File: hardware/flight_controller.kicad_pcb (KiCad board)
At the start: 6 copper layers, 50 x 50 mm, 81 parts, among them IC2 STM32F722RET6, IC3 W25Q128JVSIQ, J1 Conn_01x03, J2 Conn_01x08, J3 Conn_01x04, J4 Conn_01x04, J5 Conn_01x04, J6 USB4105-GF-A-060, Q1 TPRT9013-33GB, SW2 SW_SPST, U1 BMP581, U2 MP9943GQ-Z, U3 USBLC6-2P6, U4 MP9943GQ-Z, Y2 X322525MOB4SI

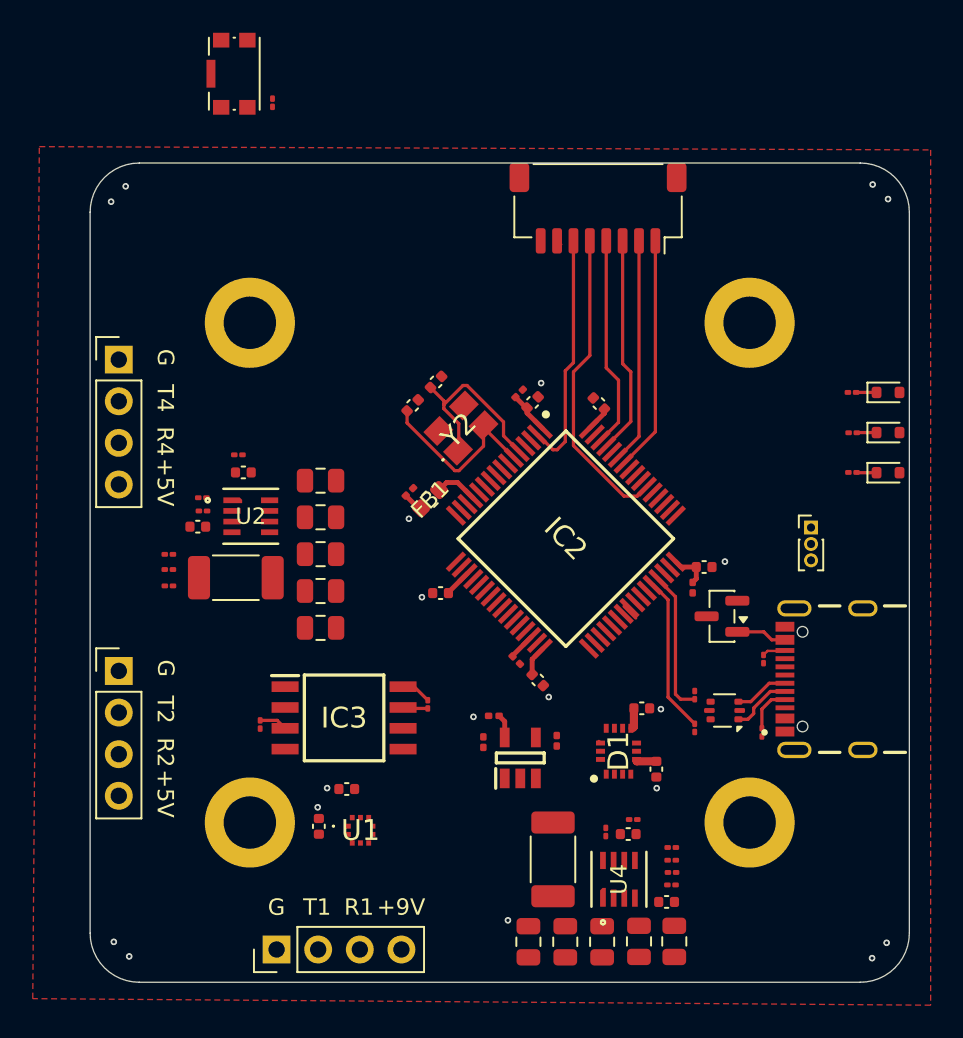
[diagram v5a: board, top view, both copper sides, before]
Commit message: redefined signal layout
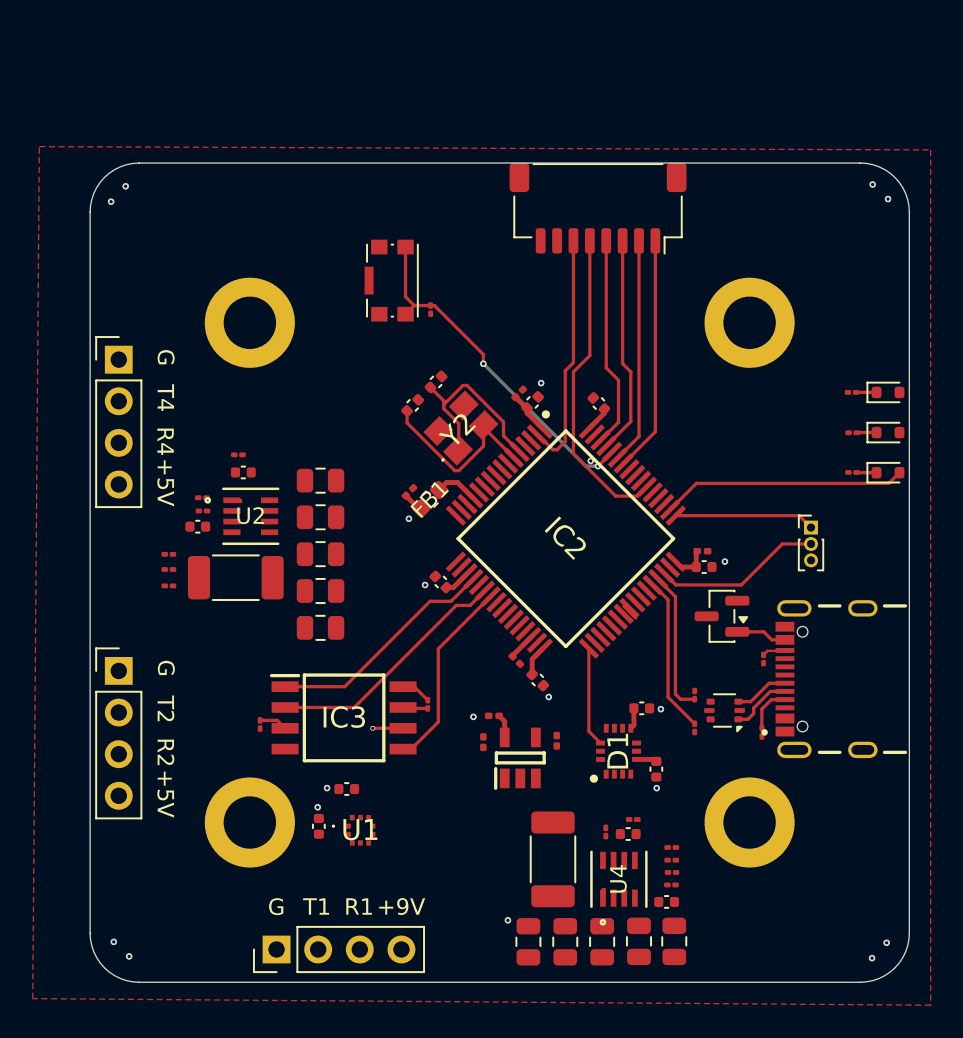
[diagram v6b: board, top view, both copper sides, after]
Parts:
- moved R22 15.9 mm to (170.3, 88.9)
- moved SW2 15.9 mm to (168.0, 87.2)
- moved C29 2.30 mm to (186.9, 103.7), turned to 180 degrees
- moved C24 0.68 mm to (170.9, 105.6), turned to -45 degrees
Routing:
- net /BOOT: track 0.00 -> 21.4 mm, vias 0 -> 3
- net /FLASH_MISO: track 0.00 -> 15.1 mm
- net /STATUS: track 0.00 -> 14.9 mm
- net /CS_FLASH: track 0.00 -> 14.2 mm
- net /FLASH_MOSI: track 0.00 -> 11.8 mm
- net /JTAG_SWDIO: track 0.00 -> 10.3 mm
- net /JTAG_SWCLK: track 0.00 -> 8.56 mm
- net /ICM_CS: track 0.14 -> 6.06 mm
- net /FLASH_SCLK: track 0.00 -> 1.85 mm, vias 0 -> 1

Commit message: redefined signal layout
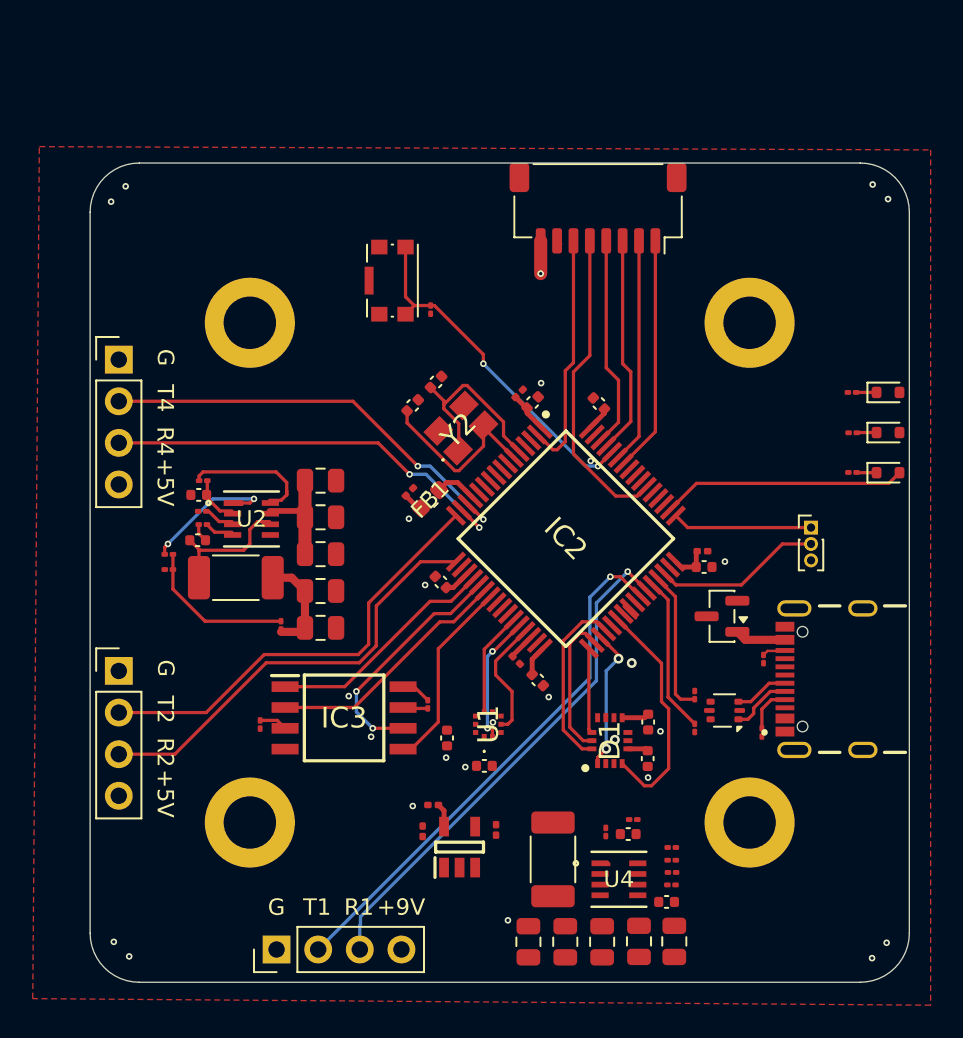
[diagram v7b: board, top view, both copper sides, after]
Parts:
- moved C20 10.8 mm to (173.6, 116.8), turned to 180 degrees
- moved U1 10.1 mm to (173.8, 114.3), turned to 90 degrees
- moved R7 7.25 mm to (161.2, 108.2), turned to -90 degrees
- moved C19 6.87 mm to (171.3, 115.1), turned to -90 degrees
- moved C8 6.58 mm to (174.3, 120.7)
- moved C30 6.58 mm to (170.4, 119.2)
- moved C9 6.58 mm to (169.8, 120.8)
- moved Q1 6.58 mm to (172.1, 121.8)
- moved C4 3.05 mm to (156.1, 100.3), turned to 180 degrees
- moved R3 2.66 mm to (156.4, 99.4), turned to 0 degrees
- moved C21 0.92 mm to (183.6, 114.1), turned to -90 degrees
- moved C22 0.83 mm to (183.5, 116.3)
- moved D1 0.83 mm to (181.2, 115.3)
- moved R4 0.83 mm to (156.3, 101.3)
- moved C5 0.83 mm to (156.1, 103.0)
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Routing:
- net /VTX_TX: track 0.00 -> 32.5 mm, vias 0 -> 1
- net /VTX_RX: track 0.00 -> 31.5 mm, vias 0 -> 1
- net /TRANSCEIVER_TX: track 0.00 -> 27.0 mm
- net /TRANSCEIVER_RX: track 0.00 -> 26.9 mm
- net /GPS_TX: track 0.00 -> 26.6 mm, vias 0 -> 2
- net /GPS_RX: track 0.00 -> 25.7 mm, vias 0 -> 2
- net /ICM_INT1: track 0.00 -> 14.2 mm
- net /FLASH_SCLK: track 1.85 -> 14.7 mm, vias 1 -> 4
- net /ICM_MOSI: track 0.00 -> 11.0 mm
- net Net-(R6-Pad2): track 0.00 -> 9.53 mm
- net VBAT: track 0.00 -> 8.80 mm, vias 0 -> 1
- net /ICM_SCLK: track 0.05 -> 8.85 mm
- net /ICM_MISO: track 0.00 -> 8.71 mm, vias 0 -> 4
- net Net-(U2-PG): track 0.00 -> 8.19 mm
- net Net-(U2-SW): track 0.00 -> 8.06 mm
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
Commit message: redefined signal layout
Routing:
- added copper zone on In2.Cu, net +3.3V
- added copper zone on In2.Cu, net +5V
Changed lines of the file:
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@@
+	)
+	(zone
+		(net 5)
+		(net_name "+3.3V")
+		(layer "In2.Cu")
+		(hatch edge 0.5)
+		(priority 3)
+		(connect_pads
+			(clearance 0.2)
+		)
+		(min_thickness 0.25)
+		(filled_areas_thickness no)
+		(fill yes
+			(thermal_gap 0.5)
+			(thermal_bridge_width 0.5)
+		)
+		(polygon
+			(pts
+				(xy 161 79) (xy 161.25 121.5) (xy 189.25 121.5) (xy 189 95) (xy 199.5 95) (xy 199.75 79.25)
+			)
+		)
+	)
+	(zone
+		(net 52)
+		(net_name "+5V")
+		(layer "In2.Cu")
+		(hatch edge 0.5)
+		(priority 4)
+		(connect_pads
+			(clearance 0.2)
+		)
+		(min_thickness 0.25)
+		(filled_areas_thickness no)
+		(fill
+			(thermal_gap 0.5)
+			(thermal_bridge_width 0.5)
+		)
+		(polygon
+			(pts
+				(xy 145.75 79) (xy 201 79.25) (xy 199.75 131) (xy 146 131)
+			)
+		)
 	)
 	(zone
